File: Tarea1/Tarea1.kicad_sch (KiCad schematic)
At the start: 10 parts, among them J1 Conn_01x02_Socket, J2 Conn_01x02_Socket, U1 LM2596T-ADJ

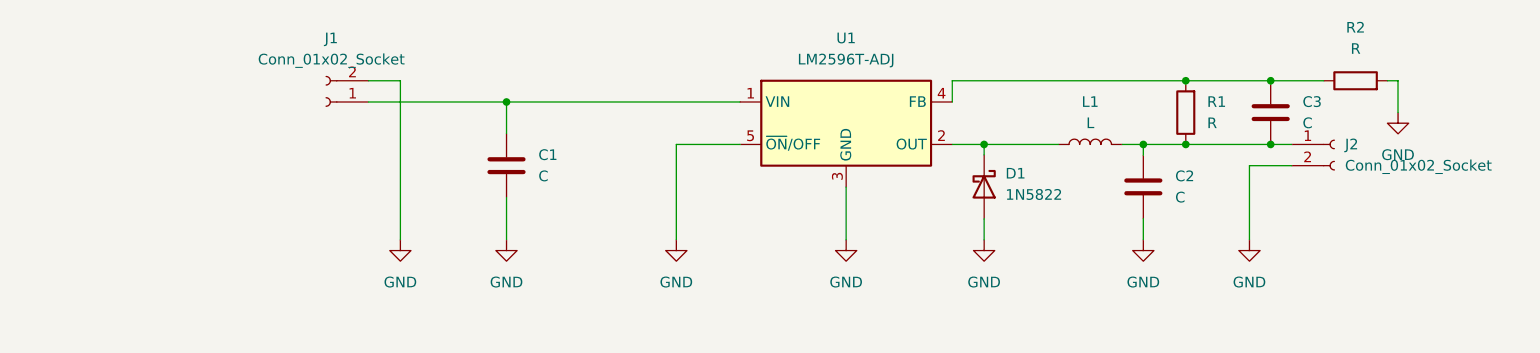
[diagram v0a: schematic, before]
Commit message: Diseño de PCB sobre un conversor reductor
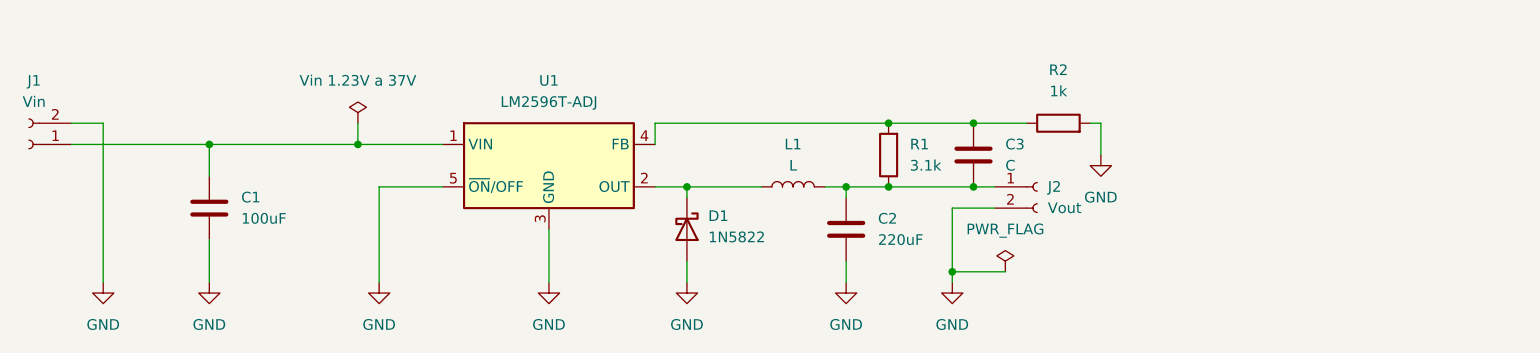
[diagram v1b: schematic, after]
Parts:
- C1: value C -> 100uF
- C2: value C -> 220uF
- J1: value Conn_01x02_Socket -> Vin
- J2: value Conn_01x02_Socket -> Vout
- L1: footprint Inductor_SMD:L_6.3x6.3_H3 -> Inductor_SMD:L_Cenker_CKCS8080
- R1: value R -> 3.1k
- R2: value R -> 1k
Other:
- company: (none) -> UCB
- title: (none) -> Step down Voltaje Converter
- moved on the sheet: C1, C2, C3, D1, J1, J2, L1, R1, R2, U1

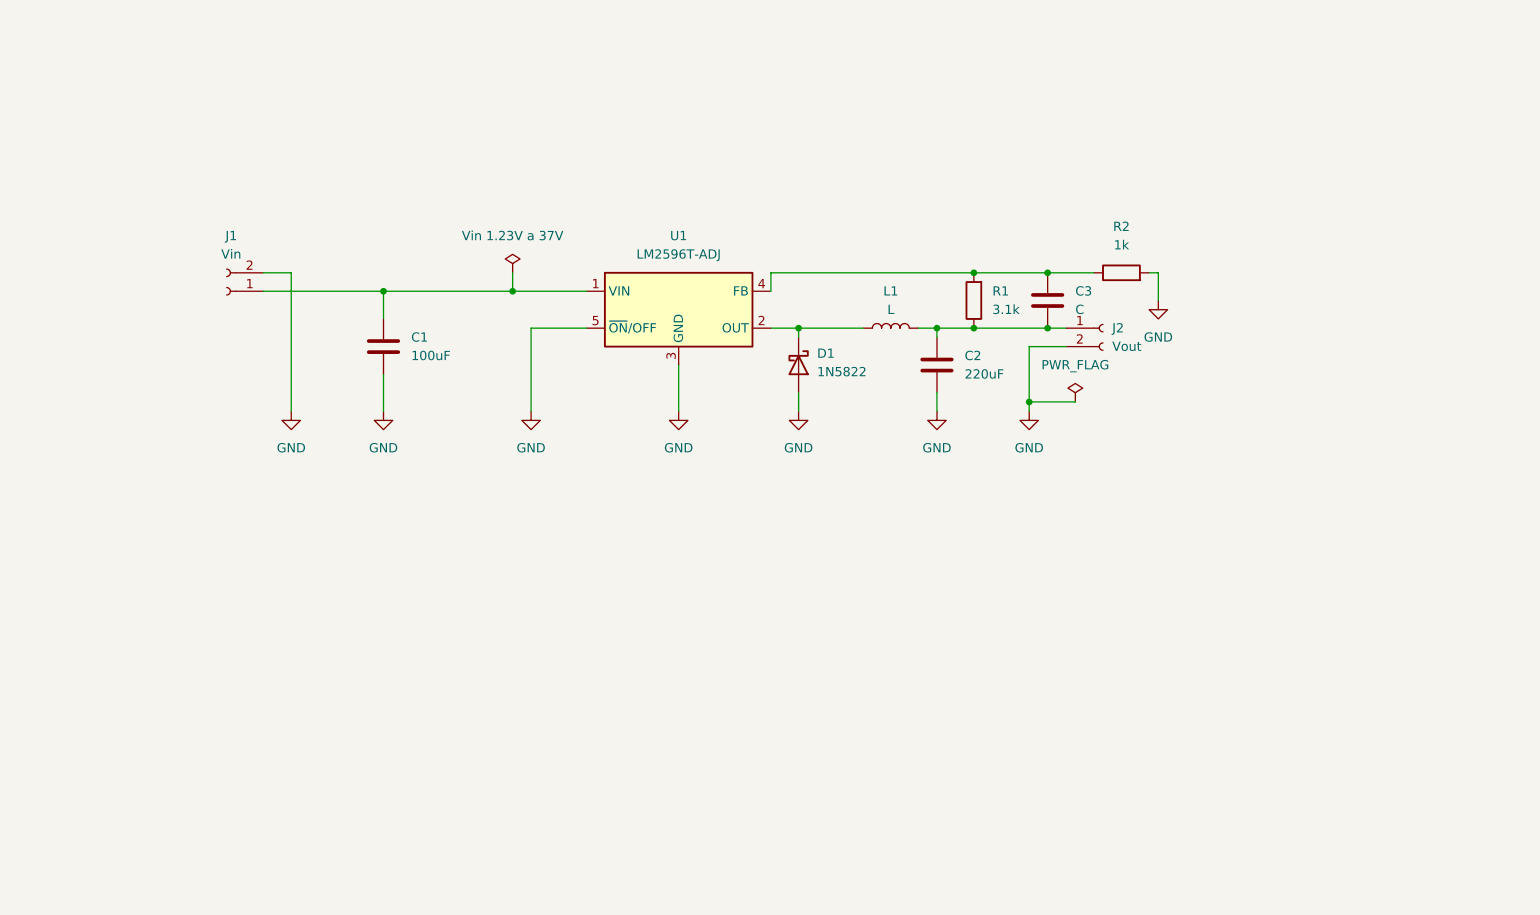
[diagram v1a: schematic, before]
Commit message: Diseño PCB de convertidor reductor de voltaje
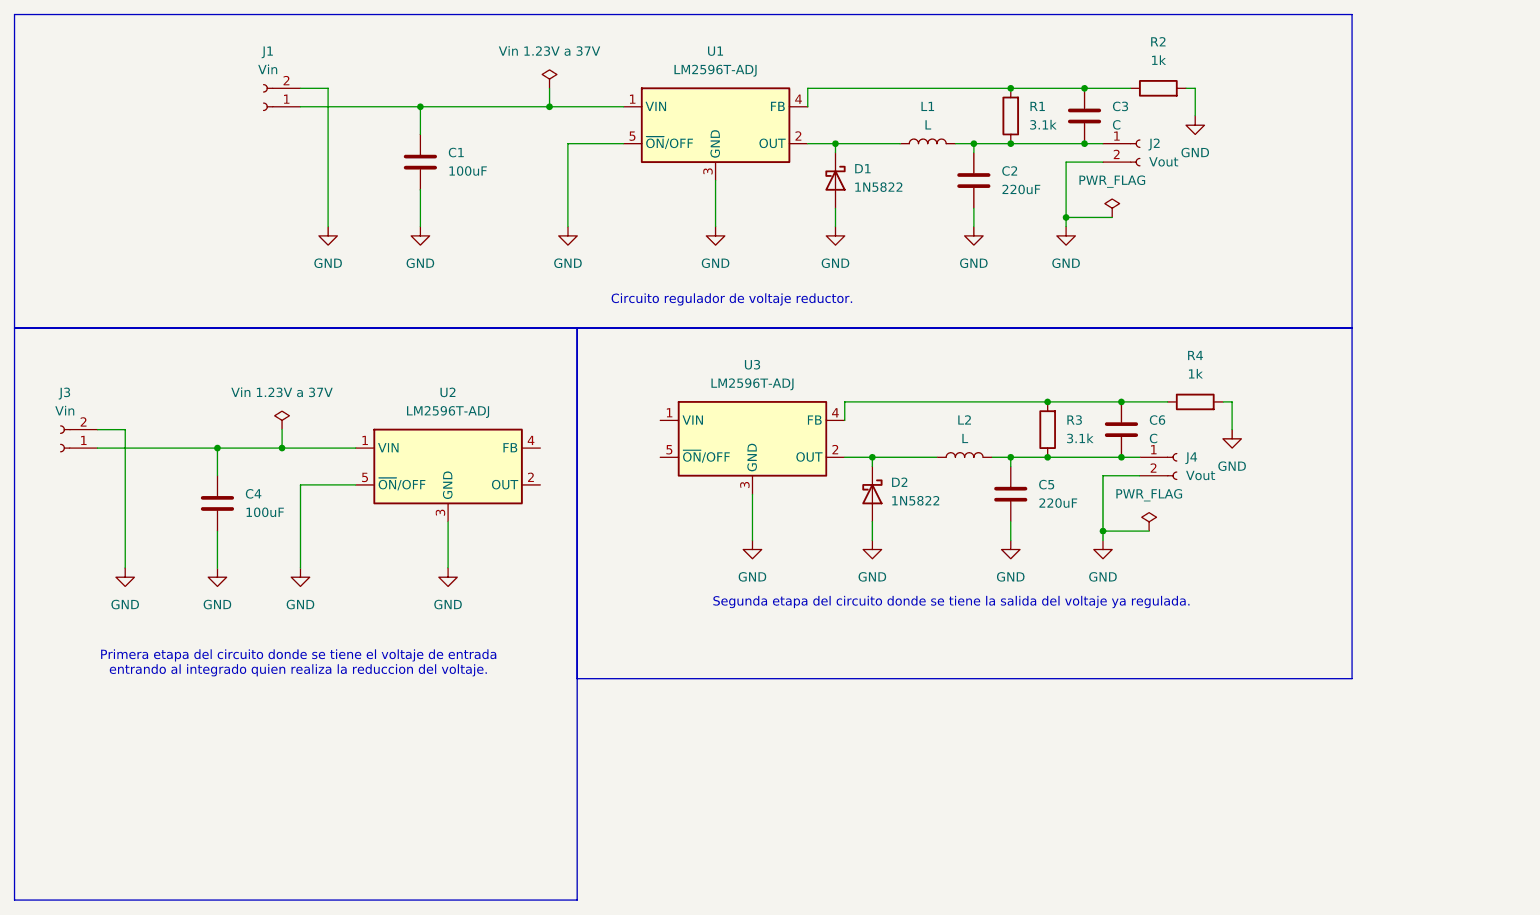
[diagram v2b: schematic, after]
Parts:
- added C4: 100uF, Capacitor_SMD:C_1210_3225Metric, symbol Device:C
- added C5: 220uF, Capacitor_SMD:C_1210_3225Metric, symbol Device:C
- added C6: C, Capacitor_SMD:C_1210_3225Metric, symbol Device:C
- added D2: 1N5822, Diode_THT:D_DO-201AD_P5.08mm_Vertical_KathodeUp, symbol Diode:1N5822
- added J3: Vin, Connector_Wire:SolderWire-1.5sqmm_1x02_P6mm_D1.7mm_OD3mm, symbol Connector:Conn_01x02_Socket
- added J4: Vout, Connector_Wire:SolderWire-1.5sqmm_1x02_P6mm_D1.7mm_OD3mm, symbol Connector:Conn_01x02_Socket
- added L2: L, Inductor_SMD:L_Cenker_CKCS8080, symbol Device:L
- added R3: 3.1k, Resistor_SMD:R_0805_2012Metric, symbol Device:R
- added R4: 1k, Resistor_SMD:R_0805_2012Metric, symbol Device:R
- added U2, U3: LM2596T-ADJ, Package_TO_SOT_THT:TO-220-5_P3.4x3.7mm_StaggerOdd_Lead3.8mm_Vertical, symbol Regulator_Switching:LM2596T-ADJ
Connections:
- net GND: now also C4.2, C5.2, D2.2 (A), J3.2 (Pin_2), J4.2 (Pin_2), R4.2, U2.3 (GND), U2.5 (~{ON}/OFF), U3.3 (GND)
- new net: D2.1 (K), L2.1, U3.2 (OUT)
- new net: C5.1, C6.2, J4.1 (Pin_1), L2.2, R3.1
- new net: C6.1, R3.2, R4.1, U3.4 (FB)
- new net: C4.1, J3.1 (Pin_1), U2.1 (VIN)
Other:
- note added: "Circuito regulador de voltaje reductor."
- note added: "Primera etapa del circuito donde se tiene el voltaje de entrada entrando al integrado quien realiza la reduccion del voltaje."
- note added: "Segunda etapa del circuito donde se tiene la salida del voltaje ya regulada."
- moved on the sheet: C1, C2, C3, D1, J1, J2, L1, R1, R2, U1
